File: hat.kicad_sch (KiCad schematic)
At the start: 7 parts, among them J1 GPIO, J8 Conn_01x02, U1 CAT24C256

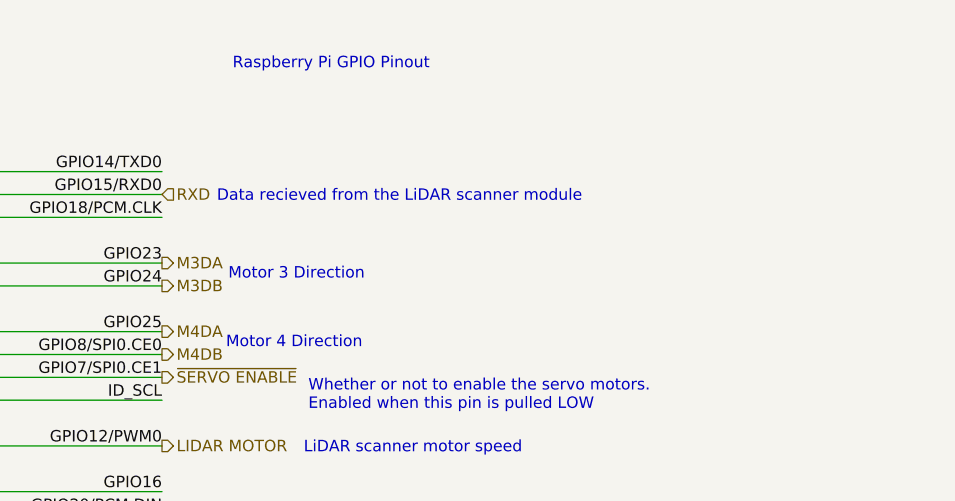
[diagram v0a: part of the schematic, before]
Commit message: feat(pcb): made the fan controlled by a NPN transistor
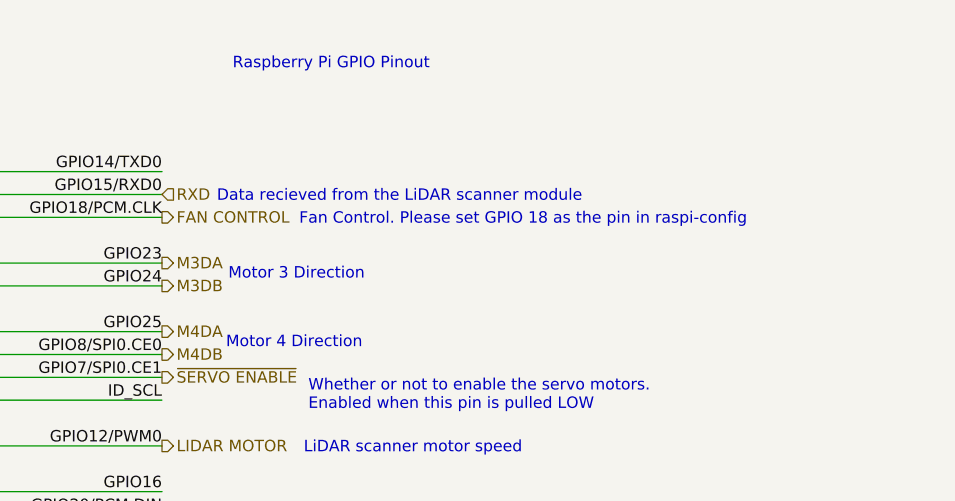
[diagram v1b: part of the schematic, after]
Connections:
- net GPIO18/PCM.CLK renamed FAN CONTROL
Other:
- note added: "Fan Control. Please set GPIO 18 as the pin in raspi-config"
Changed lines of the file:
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@@
+		)
+	)
+	(text "Fan Control. Please set GPIO 18 as the pin in raspi-config"
+		(exclude_from_sim no)
+		(at 193.04 77.724 0)
+		(effects
+			(font
+				(size 1.27 1.27)
+			)
+			(justify left)
 		)
 	)
@@
 		)
 	)
+	(hierarchical_label "FAN CONTROL"
+		(shape output)
+		(at 177.8 77.47 0)
+		(effects
+			(font
+				(size 1.27 1.27)
+			)
+			(justify left)
+		)
+	)

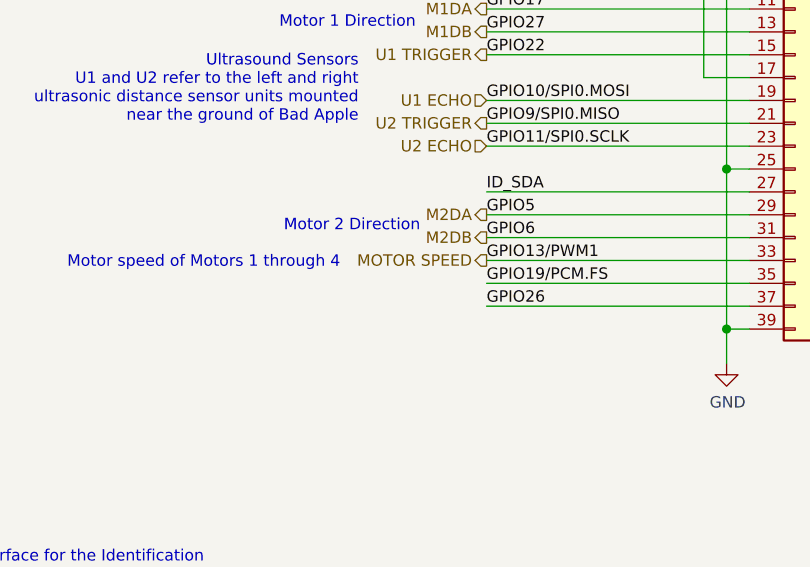
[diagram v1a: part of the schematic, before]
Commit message: doc(pcb): added docs for some of the main components of the HAT
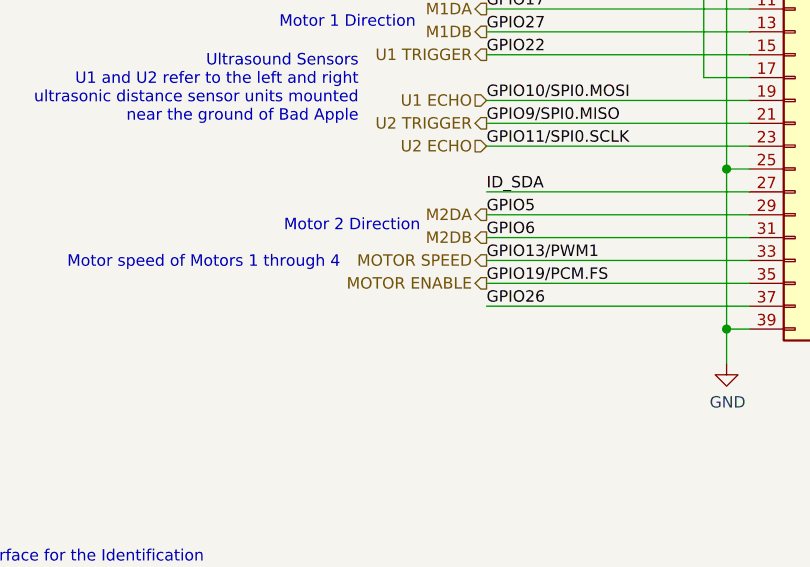
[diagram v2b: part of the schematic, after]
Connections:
- net GPIO19/PCM.FS renamed MOTOR ENABLE
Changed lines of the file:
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@@
+		)
+	)
+	(hierarchical_label "MOTOR ENABLE"
+		(shape output)
+		(at 109.22 107.95 180)
+		(effects
+			(font
+				(size 1.27 1.27)
+			)
+			(justify right)
 		)
 	)

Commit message: chore(pcb)??: i forgor what this commit does lmao
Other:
- note added: "Motor Enable. This is pulled LOW by default, and must be pulled HIGH when the robot should begin to move"
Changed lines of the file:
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@@
+		)
+	)
+	(text "Motor Enable. This is pulled LOW by default, and\nmust be pulled HIGH when the robot should begin\nto move"
+		(exclude_from_sim no)
+		(at 92.964 109.982 0)
+		(effects
+			(font
+				(size 1.27 1.27)
+			)
+			(justify right)
 		)
 	)

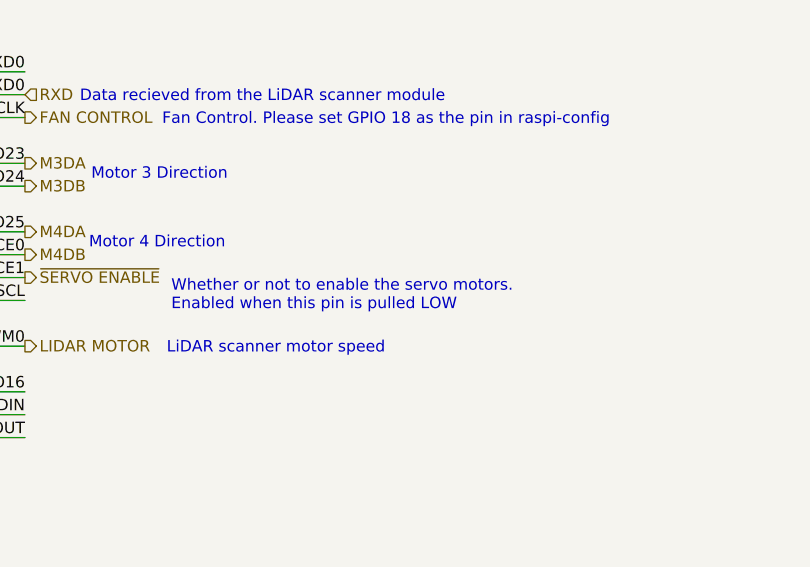
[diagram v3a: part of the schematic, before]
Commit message: feat(pcb): (somewhat) finalized all the parts needed
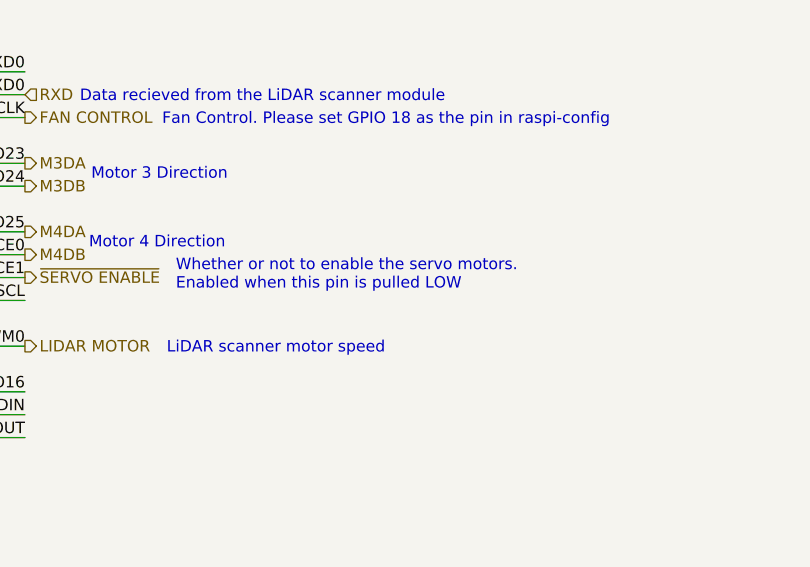
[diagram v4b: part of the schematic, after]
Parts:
- C1: footprint (none) -> Capacitor_SMD:C_0805_2012Metric
- J8: footprint (none) -> Connector_PinHeader_2.54mm:PinHeader_1x02_P2.54mm_Vertical
- JP1: footprint (none) -> Jumper:SolderJumper-2_P1.3mm_Open_RoundedPad1.0x1.5mm
- R1, R2: footprint (none) -> Resistor_SMD:R_1206_3216Metric
- U1: footprint (none) -> Package_SO:SOIC-8_3.9x4.9mm_P1.27mm
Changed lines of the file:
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@@
 	(text "Whether or not to enable the servo motors.\nEnabled when this pin is pulled LOW"
 		(exclude_from_sim no)
-		(at 194.056 97.282 0)
+		(at 194.564 94.996 0)
 		(effects
 			(font
@@
 			)
 		)
-		(property "Footprint" ""
+		(property "Footprint" "Capacitor_SMD:C_0805_2012Metric"
 			(at 67.31 179.07 0)
 			(effects
@@
 			)
 		)
-		(property "Footprint" ""
+		(property "Footprint" "Resistor_SMD:R_1206_3216Metric"
 			(at 93.98 171.45 0)
 			(effects
@@
 			)
 		)
-		(property "Footprint" ""
+		(property "Footprint" "Jumper:SolderJumper-2_P1.3mm_Open_RoundedPad1.0x1.5mm"
 			(at 96.52 181.61 0)
 			(effects
@@
 			)
 		)
-		(property "Footprint" ""
+		(property "Footprint" "Resistor_SMD:R_1206_3216Metric"
 			(at 101.6 171.45 0)
 			(effects
@@
 			)
 		)
-		(property "Footprint" ""
+		(property "Footprint" "Connector_PinHeader_2.54mm:PinHeader_1x02_P2.54mm_Vertical"
 			(at 44.45 140.97 0)
 			(effects
@@
 			)
 		)
-		(property "Footprint" ""
+		(property "Footprint" "Package_SO:SOIC-8_3.9x4.9mm_P1.27mm"
 			(at 81.28 179.07 0)
 			(effects

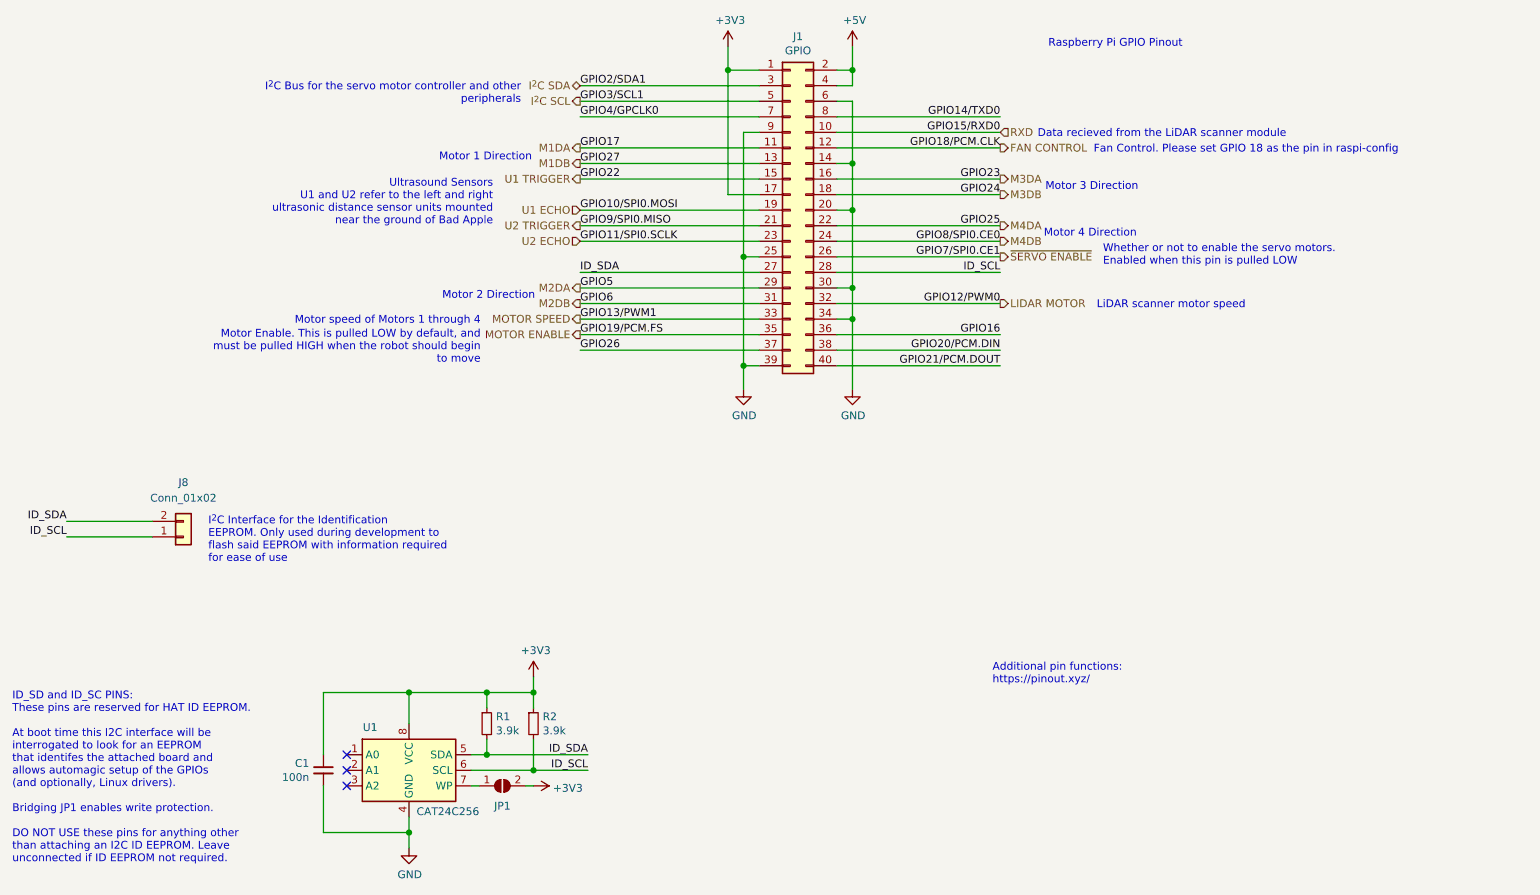
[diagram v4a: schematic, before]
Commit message: chore: cleared I2S Interface
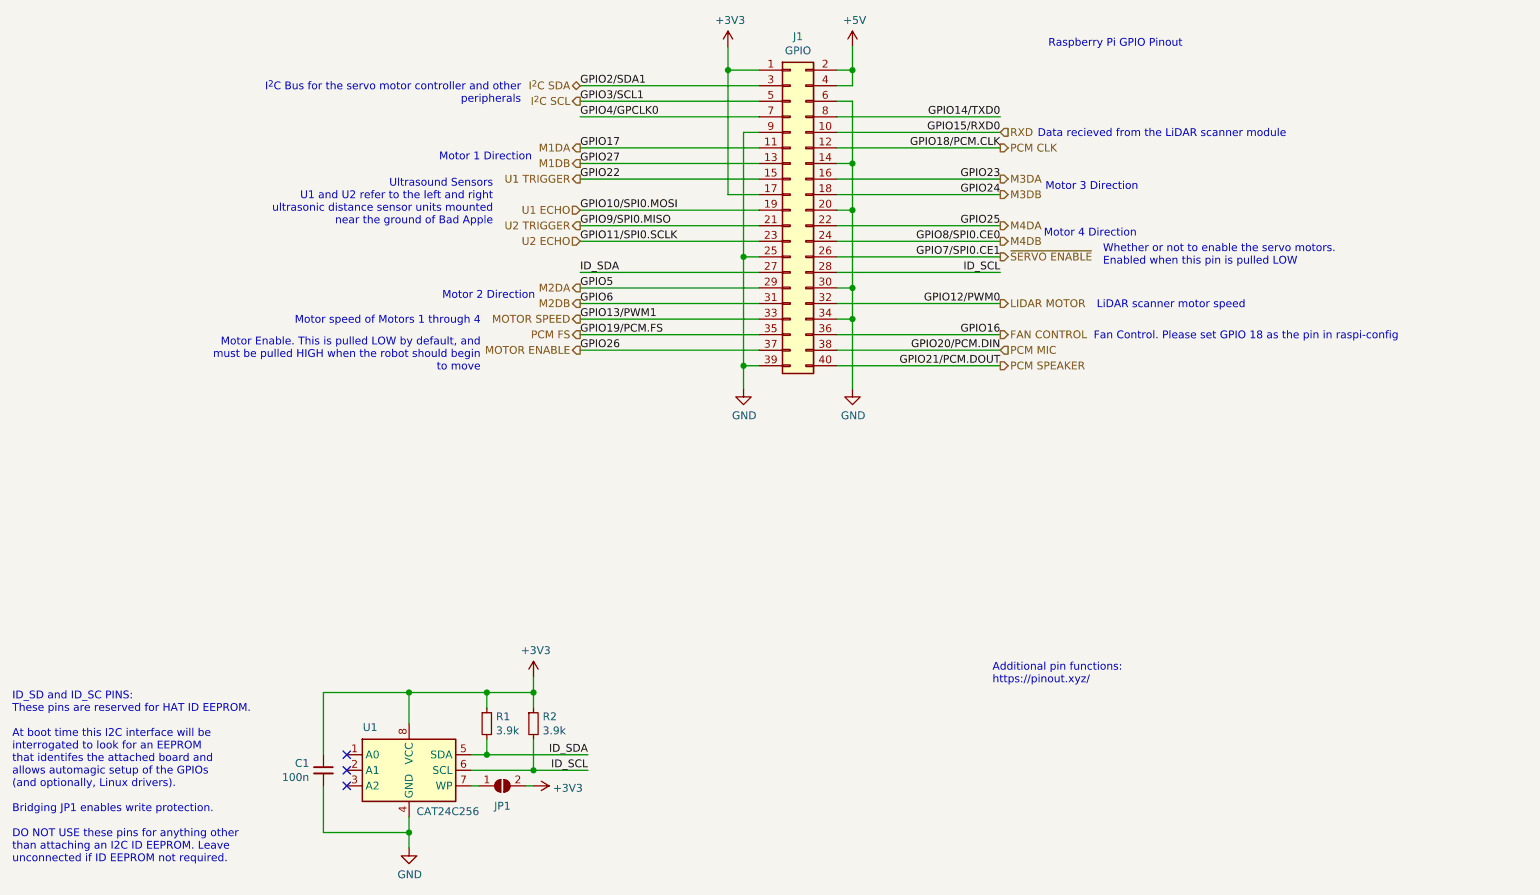
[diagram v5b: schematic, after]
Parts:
- removed J8: Conn_01x02, Connector_PinHeader_2.54mm:PinHeader_1x02_P2.54mm_Vertical, symbol Connector_Generic:Conn_01x02
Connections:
- net GPIO16 is gone; now on net FAN CONTROL: J1.36 (Pin_36)
- net GPIO26 is gone; now on net MOTOR ENABLE: J1.37 (Pin_37)
- net FAN CONTROL: no longer J1.12 (Pin_12)
- net MOTOR ENABLE: no longer J1.35 (Pin_35)
- net GPIO20/PCM.DIN renamed PCM MIC
- net GPIO21/PCM.DOUT renamed PCM SPEAKER
- new net PCM CLK: J1.12 (Pin_12)
- new net PCM FS: J1.35 (Pin_35)
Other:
- note removed: "I^{2}C Interface for the Identification EEPROM. Only used during development to flash said EEPROM with information required for ease of use"
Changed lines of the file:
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@@
+		)
+	)
+	(text "Fan Control. Please set GPIO 18 as the pin in raspi-config"
+		(exclude_from_sim no)
+		(at 193.04 108.204 0)
+		(effects
+			(font
+				(size 1.27 1.27)
+			)
+			(justify left)
 		)
 	)
@@
 		)
 	)
-	(text "Fan Control. Please set GPIO 18 as the pin in raspi-config"
-		(exclude_from_sim no)
-		(at 193.04 77.724 0)
-		(effects
-			(font
-				(size 1.27 1.27)
-			)
-			(justify left)
-		)
-	)
-	(text "I^{2}C Interface for the Identification\nEEPROM. Only used during development to\nflash said EEPROM with information required\nfor ease of use"
-		(exclude_from_sim no)
-		(at 48.514 141.478 0)
-		(effects
-			(font
-				(size 1.27 1.27)
-			)
-			(justify left)
-		)
-	)
 	(text "ID_SD and ID_SC PINS:\nThese pins are reserved for HAT ID EEPROM.\n\nAt boot time this I2C interface will be\ninterrogated to look for an EEPROM\nthat identifes the attached board and\nallows automagic setup of the GPIOs\n(and optionally, Linux drivers).\n\nBridging JP1 enables write protection.\n\nDO NOT USE these pins for anything other\nthan attaching an I2C ID EEPROM. Leave\nunconnected if ID EEPROM not required."
 		(exclude_from_sim no)
@@
 	(text "Motor Enable. This is pulled LOW by default, and\nmust be pulled HIGH when the robot should begin\nto move"
 		(exclude_from_sim no)
-		(at 92.964 109.982 0)
+		(at 92.964 111.252 0)
 		(effects
 			(font
@@
 	(wire
 		(pts
-			(xy 25.4 138.43) (xy 39.37 138.43)
-		)
-		(stroke
-			(width 0)
-			(type default)
-		)
-	)
-	(wire
-		(pts
 			(xy 138.43 67.31) (xy 109.22 67.31)
 		)
@@
 			(width 0)
 			(type solid)
-		)
-	)
-	(wire
-		(pts
-			(xy 25.4 140.97) (xy 39.37 140.97)
-		)
-		(stroke
-			(width 0)
-			(type default)
 		)
 	)
@@
 		)
 	)
-	(label "ID_SCL"
-		(at 25.4 140.97 180)
-		(effects
-			(font
-				(size 1.27 1.27)
-			)
-			(justify right bottom)
-		)
-	)
 	(label "GPIO9{slash}SPI0.MISO"
 		(at 109.22 90.17 0)
@@
 		)
 	)
-	(label "ID_SDA"
-		(at 25.4 138.43 180)
-		(effects
-			(font
-				(size 1.27 1.27)
-			)
-			(justify right bottom)
-		)
-	)
 	(label "ID_SCL"
 		(at 177.8 97.79 180)
@@
 			)
 			(justify right bottom)
-		)
-	)
-	(hierarchical_label "MOTOR ENABLE"
-		(shape output)
-		(at 109.22 107.95 180)
-		(effects
-			(font
-				(size 1.27 1.27)
-			)
-			(justify right)
 		)
 	)
@@
 		)
 	)
+	(hierarchical_label "FAN CONTROL"
+		(shape output)
+		(at 177.8 107.95 0)
+		(effects
+			(font
+				(size 1.27 1.27)
+			)
+			(justify left)
+		)
+	)
 	(hierarchical_label "U2 TRIGGER"
 		(shape output)
@@
 		)
 	)
+	(hierarchical_label "PCM MIC"
+		(shape input)
+		(at 177.8 110.49 0)
+		(effects
+			(font
+				(size 1.27 1.27)
+			)
+			(justify left)
+		)
+	)
 	(hierarchical_label "M2DA"
 		(shape output)
@@
 		)
 	)
+	(hierarchical_label "PCM CLK"
+		(shape output)
+		(at 177.8 77.47 0)
+		(effects
+			(font
+				(size 1.27 1.27)
+			)
+			(justify left)
+		)
+	)
 	(hierarchical_label "MOTOR SPEED"
 		(shape output)
@@
 		)
 	)
-	(hierarchical_label "FAN CONTROL"
-		(shape output)
-		(at 177.8 77.47 0)
-		(effects
-			(font
-				(size 1.27 1.27)
-			)
-			(justify left)
-		)
-	)
 	(hierarchical_label "I^{2}C SDA"
 		(shape bidirectional)
@@
 		)
 	)
+	(hierarchical_label "PCM SPEAKER"
+		(shape output)
+		(at 177.8 113.03 0)
+		(effects
+			(font
+				(size 1.27 1.27)
+			)
+			(justify left)
+		)
+	)
+	(hierarchical_label "PCM FS"
+		(shape output)
+		(at 109.22 107.95 180)
+		(effects
+			(font
+				(size 1.27 1.27)
+			)
+			(justify right)
+		)
+	)
 	(hierarchical_label "M4DB"
 		(shape output)
@@
 			)
 			(justify left)
+		)
+	)
+	(hierarchical_label "MOTOR ENABLE"
+		(shape output)
+		(at 109.22 110.49 180)
+		(effects
+			(font
+				(size 1.27 1.27)
+			)
+			(justify right)
 		)
 	)
@@
 					(unit 1)
 				)
-			)
-		)
-	)
-	(symbol
-		(lib_id "Connector_Generic:Conn_01x02")
-		(at 44.45 140.97 0)
-		(mirror x)
-		(unit 1)
-		(exclude_from_sim no)
-		(in_bom yes)
-		(on_board yes)
-		(dnp no)
-		(property "Reference" "J8"
-			(at 44.45 132.08 0)
-			(effects
-				(font
-					(size 1.27 1.27)
-				)
-			)
-		)
-		(property "Value" "Conn_01x02"
-			(at 44.45 134.62 0)
-			(effects
-				(font
-					(size 1.27 1.27)
-				)
-			)
-		)
-		(property "Footprint" "Connector_PinHeader_2.54mm:PinHeader_1x02_P2.54mm_Vertical"
-			(at 44.45 140.97 0)
-			(effects
-				(font
-					(size 1.27 1.27)
-				)
-				(hide yes)
-			)
-		)
-		(property "Datasheet" "~"
-			(at 44.45 140.97 0)
-			(effects
-				(font
-					(size 1.27 1.27)
-				)
-				(hide yes)
-			)
-		)
-		(property "Description" "Generic connector, single row, 01x02, script generated (kicad-library-utils/schlib/autogen/connector/)"
-			(at 44.45 140.97 0)
-			(effects
-				(font
-					(size 1.27 1.27)
-				)
-				(hide yes)
-			)
-		)
-		(pin "1"
-		)
-		(pin "2"
-		)
-		(instances
-			(project ""
-				(path "/e63e39d7-6ac0-4ffd-8aa3-1841a4541b55/b30abb3a-5689-47ca-b698-70986eaac049"
-					(reference "J8")
-					(unit 1)
-				)
